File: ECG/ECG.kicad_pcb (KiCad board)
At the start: 4 copper layers, 81.3 x 109.2 mm, 80 parts, among them J1 Conn_01x03, J2 Conn_01x03, J3 Conn_01x15, J4 Conn_01x15, J5 Conn_01x02, J6 Conn_01x02, J7 Conn_01x02, J8 Conn_02x05_Odd_Even, Q1 DMG2301L, Q2 T2N7002AK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

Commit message: wip
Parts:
- J8: footprint Connector_PinSocket_2.54mm:PinSocket_2x05_P2.54mm_Vertical -> Connector_PinHeader_2.54mm:PinHeader_2x05_P2.54mm_Vertical
- moved J8 8.20 mm to (99.8, 64.3), turned to 0 degrees
- turned J5 to 90 degrees
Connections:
- J5 pad 1: Net-(D3-A) -> GND
- J5 pad 2: GND -> Net-(D3-A)
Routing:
- net /LEADS_ON: track 27.7 -> 42.0 mm, vias 0 -> 1
- net /OUT: track 62.6 -> 56.4 mm
- net /PWR_OFF_HV: track 45.4 -> 46.9 mm
- net Net-(D2-K): vias 0 -> 1

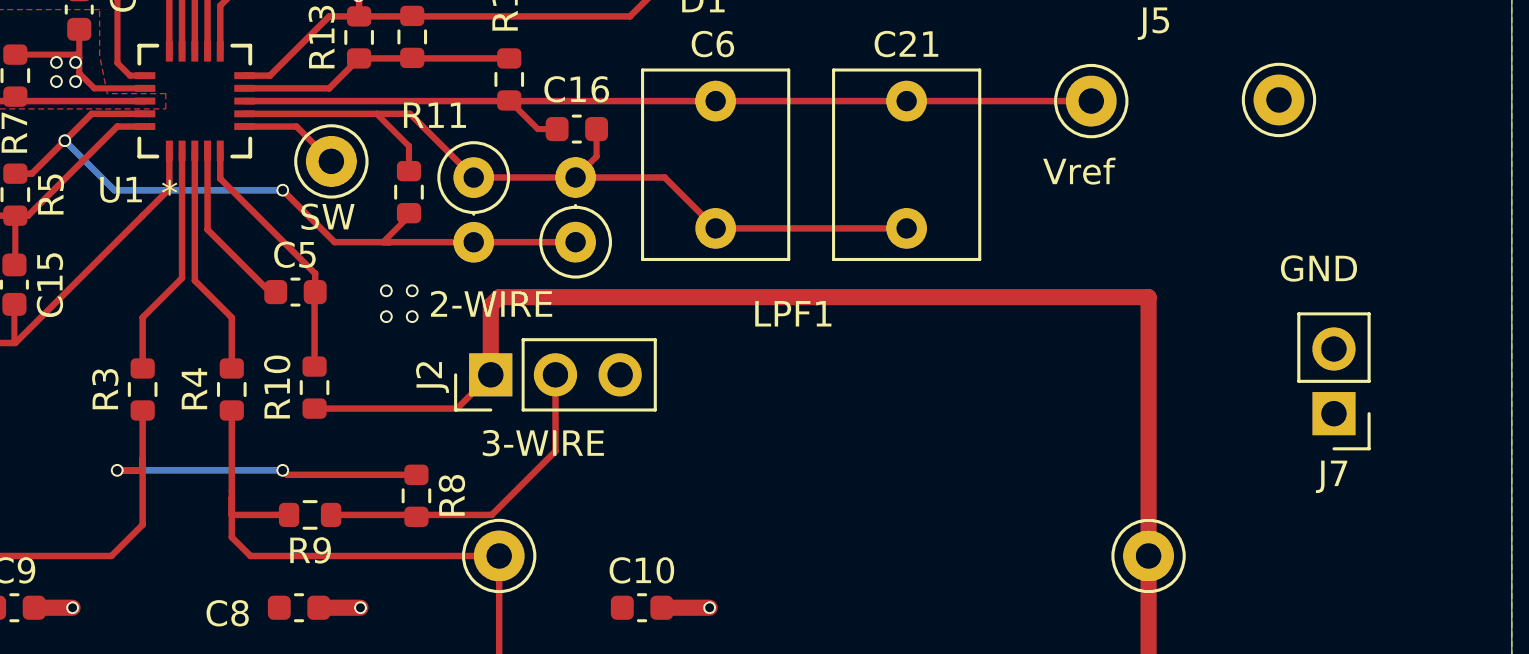
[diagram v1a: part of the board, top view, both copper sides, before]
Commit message: Remove paste from finger pads.
new gerbers
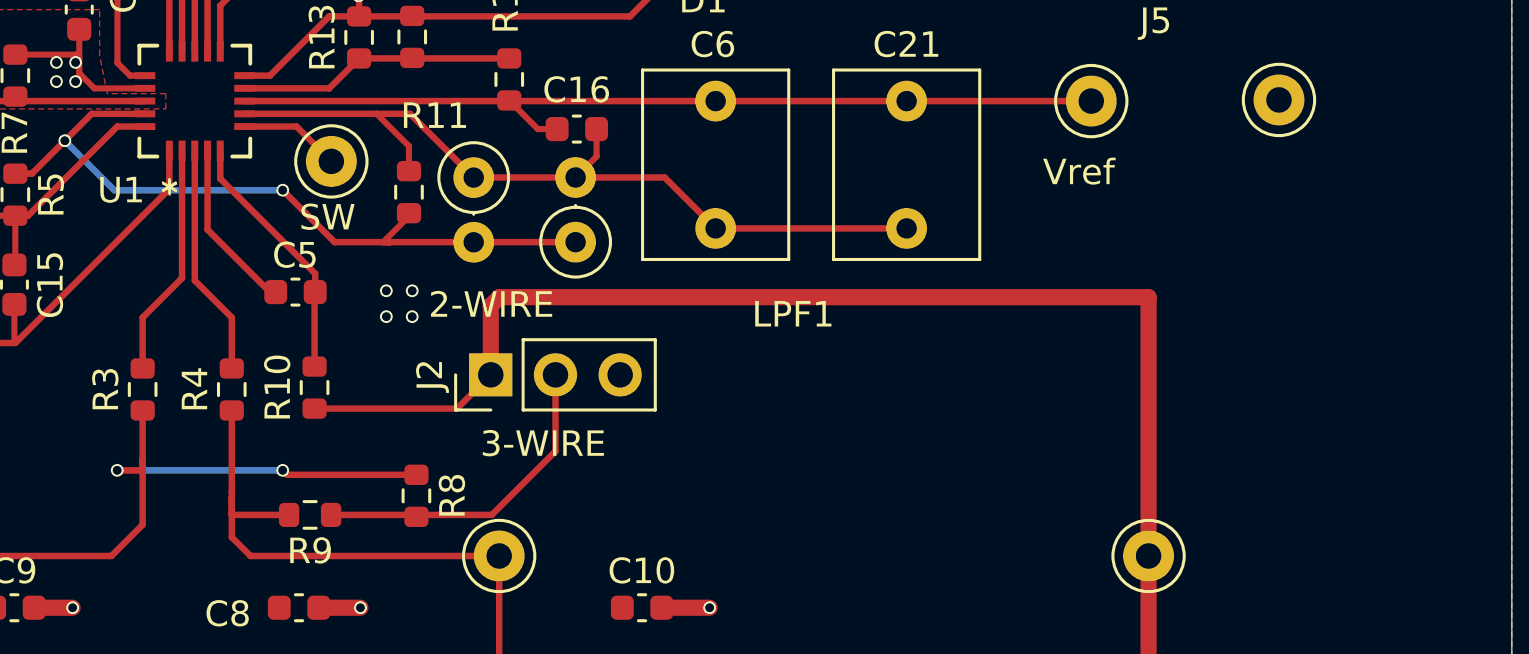
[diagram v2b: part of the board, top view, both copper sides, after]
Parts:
- removed J7: Conn_01x02, Connector_PinHeader_2.54mm:PinHeader_1x02_P2.54mm_Vertical

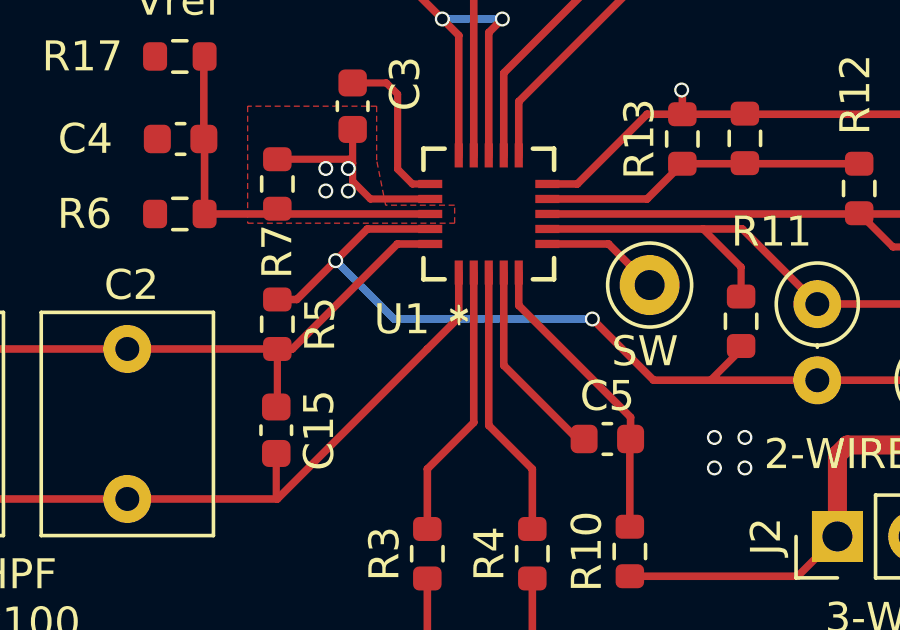
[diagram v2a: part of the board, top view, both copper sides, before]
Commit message: Replace 3 THD comps with the SMD versions in the callout box.
Remove old revision tracker.

Fix latent overlapping silkscreen error.
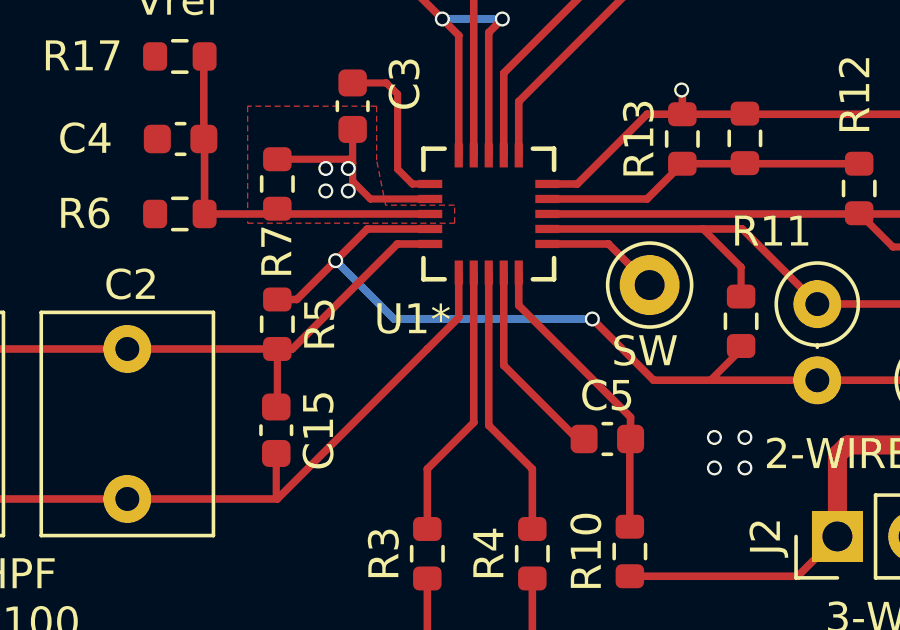
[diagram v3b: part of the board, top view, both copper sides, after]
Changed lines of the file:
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@@
 		(sheetname "/")
 		(sheetfile "ECG.kicad_sch")
-		(attr smd dnp)
+		(attr smd)
 		(fp_line
 			(start -0.237258 0.5225)
@@
 			)
 		)
+		(property "DigikeyPN" "399-5455-1-ND"
+			(at 0 0 90)
+			(unlocked yes)
+			(layer "F.Fab")
+			(hide yes)
+			(effects
+				(font
+					(size 1 1)
+					(thickness 0.15)
+				)
+			)
+		)
 		(property ki_fp_filters "C_*")
 		(sheetname "/")
 		(sheetfile "ECG.kicad_sch")
-		(attr through_hole)
+		(attr through_hole dnp)
 		(fp_line
 			(start 6.22 -2.87)
@@
 			)
 		)
+		(property "DigikeyPN" "399-5905-ND"
+			(at 0 0 90)
+			(unlocked yes)
+			(layer "F.Fab")
+			(hide yes)
+			(effects
+				(font
+					(size 1 1)
+					(thickness 0.15)
+				)
+			)
+		)
 		(property ki_fp_filters "C_*")
 		(sheetname "/")
 		(sheetfile "ECG.kicad_sch")
-		(attr through_hole)
+		(attr through_hole dnp)
 		(fp_line
 			(start 6.22 -2.87)
@@
 			)
 		)
+		(property "DigikeyPN" "2057-PH2-10-UA-ND"
+			(at 0 0 0)
+			(unlocked yes)
+			(layer "F.Fab")
+			(hide yes)
+			(effects
+				(font
+					(size 1 1)
+					(thickness 0.15)
+				)
+			)
+		)
 		(property ki_fp_filters "Connector*:*_2x??_*")
 		(sheetname "/")
@@
 			)
 		)
-		(property "Manufacturer_PN" ""
+		(property "Manufacturer_PN" "CL10B472KB8NNNC"
+			(at 0 0 180)
+			(unlocked yes)
+			(layer "F.Fab")
+			(hide yes)
+			(effects
+				(font
+					(size 1 1)
+					(thickness 0.15)
+				)
+			)
+		)
+		(property "DigikeyPN" "1276-1098-1-ND"
 			(at 0 0 180)
 			(unlocked yes)
@@
 		(sheetname "/")
 		(sheetfile "ECG.kicad_sch")
-		(attr smd dnp)
+		(attr smd)
 		(fp_line
 			(start -0.14058 0.51)
@@
 		(sheetname "/")
 		(sheetfile "ECG.kicad_sch")
-		(attr smd dnp)
+		(attr smd)
 		(fp_line
 			(start -0.14058 0.51)
@@
 			)
 		)
-		(property "DigikeyPN" "RMCF0603FT470KCT-ND"
+		(property "DigikeyPN" "13-MFR-25FTE52-470KCT-ND"
 			(at 0 0 270)
 			(unlocked yes)
@@
 		(sheetname "/")
 		(sheetfile "ECG.kicad_sch")
-		(attr through_hole)
+		(attr through_hole dnp)
 		(fp_line
 			(start 1.37 0)
@@
 		)
 		(fp_text user "*"
-			(at 1 -3.0954 180)
-			(unlocked yes)
-			(layer "F.SilkS")
-			(effects
-				(font
-					(size 1 1)
-					(thickness 0.15)
-				)
-			)
-		)
-		(fp_text user "*"
-			(at 0.987602 -3.639 180)
+			(at 1.597202 -3.5374 180)
 			(layer "F.SilkS")
 			(effects

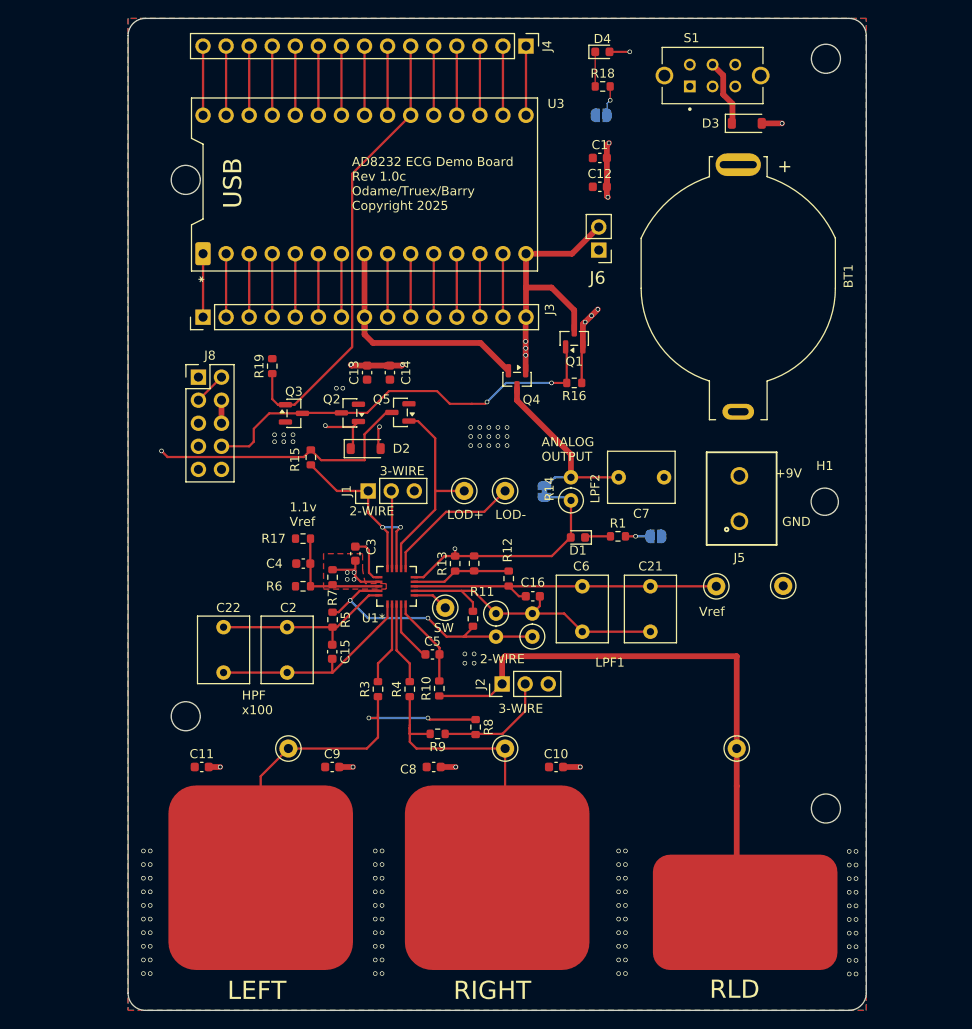
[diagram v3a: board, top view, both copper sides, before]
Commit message: Start looking at footprints and placements.
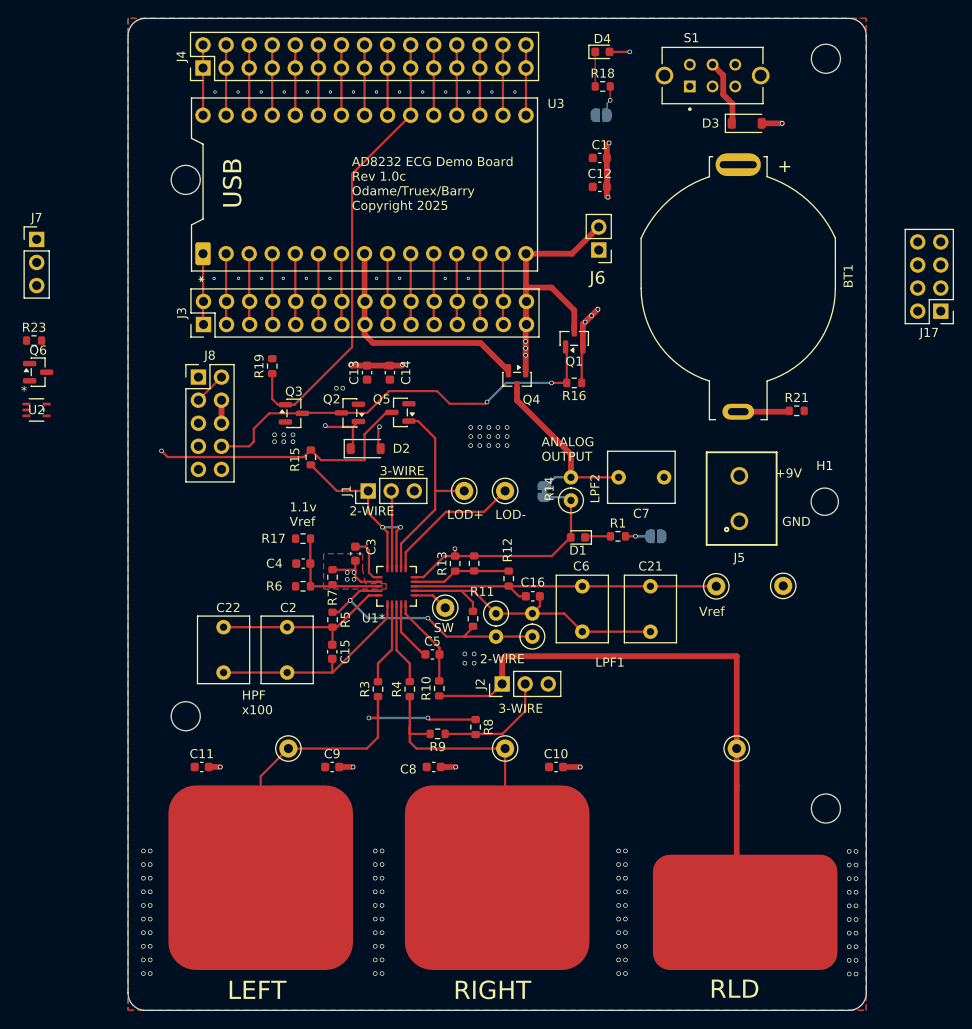
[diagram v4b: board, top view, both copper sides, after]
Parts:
- added J17: Conn_02x04_Odd_Even, Connector_PinHeader_2.54mm:PinHeader_2x04_P2.54mm_Vertical, F.Cu at (181.6, 57.0)
- added J7: Conn_01x03, Connector_PinHeader_2.54mm:PinHeader_1x03_P2.54mm_Vertical, F.Cu at (82.0, 49.1)
- added Q6: T2N7002AK, Package_TO_SOT_SMD:SOT-23, F.Cu at (82.2, 63.7)
- added R21: 1, Resistor_SMD:R_0603_1608Metric, F.Cu at (165.7, 68.0)
- added R23: 1, Resistor_SMD:R_0603_1608Metric, F.Cu at (81.7, 60.2)
- added U2: MIC920YC5-TR, StockedComponents:SC-70_C5_MCH, F.Cu at (82.0, 67.9)
- J3, J4: value Conn_01x15 -> Conn_02x15_Odd_Even; footprint Connector_PinHeader_2.54mm:PinHeader_1x15_P2.54mm_Vertical -> Connector_PinHeader_2.54mm:PinHeader_2x15_P2.54mm_Vertical
- moved J4 35.6 mm to (100.3, 30.2), turned to 90 degrees
- moved J3 0.81 mm to (100.4, 58.5)
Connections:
- BT1 pad N: GND -> /3VSens
- J3 pad 10: /A6 -> /A1
- J3 pad 11: /A7 -> /A2
- J3 pad 12: +5V -> /A2
- J3 pad 13: /RESET -> /A3
- J3 pad 14: GND -> /A3
- J3 pad 15: /VIN -> /HR_SIGNAL
- J3 pad 2: +3V3 -> /D13
- J3 pad 3: /AREF -> +3V3
- J3 pad 4: /A0 -> +3V3
- J3 pad 5: /A1 -> /AREF
- J3 pad 6: /A2 -> /AREF
- J3 pad 7: /A3 -> /A0
- J3 pad 8: /HR_SIGNAL -> /A0
- J3 pad 9: /A5 -> /A1
- J4 pad 1: /TX -> /D12
- J4 pad 10: /D7 -> /D8
- J4 pad 11: /D8 -> /D7
- J4 pad 12: /D9 -> /D7
- J4 pad 13: /D10 -> /D6
- J4 pad 14: /D11 -> /D6
- J4 pad 15: /D12 -> /D5
- J4 pad 2: /RX -> /D12
- J4 pad 3: /RESET1 -> /D11
- J4 pad 4: GND -> /D11
- J4 pad 5: /LEADS_ON_PROT -> /D10
- J4 pad 6: /PWR_HOLD -> /D10
- J4 pad 7: /D4 -> /D9
- J4 pad 8: /D5 -> /D9
- J4 pad 9: /D6 -> /D8
- J5 pad 1: GND -> /9VSens
- J8 pad 8: /PWR_OFF_HV -> /PWR_OFF_BUF
- Q4 pad 1: /VIN -> Net-(J7-Pin_2)
- Q4 pad 2: /HR_SIGNAL -> Net-(Q4-S)
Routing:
- net /3VSens: track 0.00 -> 5.66 mm
- net GND: vias 107 -> 131
